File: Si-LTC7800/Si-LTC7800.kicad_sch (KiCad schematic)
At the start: 0 parts

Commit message: Schematics for Si and GaN for LTC7800 controller
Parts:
- added BFET_VGS, TFET_VGS: TestPoint_2Pole, symbol Connector:TestPoint_2Pole
- added C1, C3, C4: 0.1uF, symbol Device:C
- added C2, CinA-1, CinA-2: 2.2uF, symbol Device:C
- added C5: 10pF, symbol Device:C
- added CinB: 56uF, symbol Device:C_US
- added Cout: 100uF, symbol Device:C
- added D1: 1N47xxA, Diode_THT:D_DO-41_SOD81_P10.16mm_Horizontal, symbol Diode:1N47xxA
- added L1: 0.3uH, XGL1010-333MED:IND_XGL1010-333MED, symbol XGL1010-333MED:XGL1010-333MED
- added Q1, Q2: DMP2045U-7, SOT96P240X115-3N, symbol DMP2045U-7:DMP2045U-7
- added R1: 100kOhm, symbol Device:R
- added R2: 25.5kOhm, symbol Device:R
- added R3: 3mOhm, symbol Device:R
- added R4: 100Ohm, symbol Device:R
- added R5: 90.9kOhm, symbol Device:R
- added R6: 280kOhm, symbol Device:R
- added TP_VIN, TP_VOUT: TestPoint, symbol Connector:TestPoint
- added U1: LTC7800HUDC_PBF, LTC7800HUDC_PBF:QFN50P400X300X80-21N, symbol LTC7800HUDC_PBF:LTC7800HUDC_PBF
- added VSource_GND, VSource_IN: 575-4, 5754, symbol 575-4:575-4
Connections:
- new net: L1.2, R3.1, R4.1
- new net: C1.2, U1.19 (TRACK/SS)
- new net: R2.2, U1.20 (FREQ)
- new net: R1.1, U1.9 (PGOOD)
- new net BG: BFET_VGS.1, Q2.1, U1.13 (BG)
- new net BOOST: C3.1, D1.1 (K), U1.12 (BOOST)
- new net GND: BFET_VGS.2, C1.1, C2.1, CinA-1.2, CinA-2.2, CinB.2, Cout.2, Q2.2, R2.1, R5.2, U1.15 (EXTVCC), U1.16 (PGND), U1.2 (SGND), U1.21 (SGND), U1.3 (SGND), VSource_GND.1
- new net INTVCC: C2.2, D1.2 (A), R1.2, U1.14 (INTVCC)
- new net SENSE+: C4.1, R4.2, U1.6 (SENSE+)
- new net SENSE-: C4.2, C5.1, Cout.1, R3.2, R6.1, TP_VOUT.1, U1.5 (SENSE-)
- new net SW: C3.2, L1.1, Q1.2, Q2.3, TFET_VGS.2, U1.11 (SW)
- new net TG: Q1.1, TFET_VGS.1, U1.10 (TG)
- new net VFB: C5.2, R5.1, R6.2, U1.7 (VFB)
- new net VIN: CinA-1.1, CinA-2.1, CinB.1, Q1.3, TP_VIN.1, U1.17 (VIN), VSource_IN.1
- no-connect marks 0 -> 4

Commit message: Updated footprints for LTC7800
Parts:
- removed D1: 1N47xxA, Diode_THT:D_DO-41_SOD81_P10.16mm_Horizontal, symbol Diode:1N47xxA
- added D1: CMPD6001_TR_PBFREE, Diode_SMD:SOT95P230X109-3N, symbol CMPD6001_TR_PBFREE:CMPD6001_TR_PBFREE
- added RLoad1: 5Ohm, Resistor_SMD:R_0201_0603Metric_Pad0.64x0.40mm_HandSolder, symbol Device:R
- BFET_VGS1: renamed from BFET_VGS; footprint (none) -> TestPoint:TestPoint_Bridge_Pitch2.54mm_Drill1.0mm
- C1, C2, C3, C4, C5, CinA-1, CinA-2: footprint (none) -> Capacitor_SMD:C_0805_2012Metric_Pad1.18x1.45mm_HandSolder
- CinB1: renamed from CinB; footprint (none) -> Capacitor_SMD:C_0805_2012Metric_Pad1.18x1.45mm_HandSolder
- Cout1: renamed from Cout; footprint (none) -> Capacitor_SMD:C_0805_2012Metric_Pad1.18x1.45mm_HandSolder
- L1: value 0.3uH -> 33uH; footprint XGL1010-333MED:IND_XGL1010-333MED -> Inductor_SMD:IND_XGL1010-333MED
- Q1, Q2: footprint SOT96P240X115-3N -> Transistor_Power:SOT96P240X115-3N
- R1, R2, R3, R4, R5, R6: footprint (none) -> Resistor_SMD:R_0201_0603Metric_Pad0.64x0.40mm_HandSolder
- TFET_VGS1: renamed from TFET_VGS; footprint (none) -> TestPoint:TestPoint_Bridge_Pitch2.54mm_Drill1.0mm
- TP_VIN1: renamed from TP_VIN; footprint (none) -> TestPoint:TestPoint_Loop_D2.60mm_Drill1.6mm_Beaded
- TP_VOUT1: renamed from TP_VOUT; footprint (none) -> TestPoint:TestPoint_Loop_D2.60mm_Drill1.6mm_Beaded
- U1: footprint LTC7800HUDC_PBF:QFN50P400X300X80-21N -> Package_DFN_QFN:QFN50P400X300X80-21N
- VSource_GND1: renamed from VSource_GND; footprint 5754 -> Battery:5754
- VSource_IN1: renamed from VSource_IN; footprint 5754 -> Battery:5754
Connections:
- net BOOST: now also D1.3 (K)
- net GND: now also RLoad1.2
- net INTVCC: now also D1.1 (A)
- net SENSE-: now also RLoad1.1
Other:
- moved on the sheet: BFET_VGS1, C1, C2, C3, C4, C5, CinA-1, CinA-2, CinB1, Cout1, L1, Q1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

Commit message: Updated shematics
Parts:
- added C6: 100pF, Capacitor_SMD:C_0805_2012Metric_Pad1.18x1.45mm_HandSolder, symbol Device:C
- added CinA-E1, CinA-E10, CinA-E11, CinA-E12, CinA-E13, CinA-E14, CinA-E2, CinA-E3, CinA-E4, CinA-E5, CinA-E6, CinA-E7, CinA-E8, CinA-E9: ~, Capacitor_SMD:C_0805_2012Metric_Pad1.18x1.45mm_HandSolder, symbol Device:C
- added R7: 33kOhm, Resistor_SMD:R_0201_0603Metric_Pad0.64x0.40mm_HandSolder, symbol Device:R
- added R9: 3.92kOhm, Resistor_SMD:R_0201_0603Metric_Pad0.64x0.40mm_HandSolder, symbol Device:R
- C1: value 0.1uF -> 0.05uF
- C5: value 10pF -> 2.2uF
- R5: value 90.9kOhm -> 6.8kOhm
- R6: value 280kOhm -> 2.7kOhm
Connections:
- net BOOST: now also CinA-E8.2
- net GND: now also C5.1, C6.1, CinA-E1.2, CinA-E10.1, CinA-E11.1, CinA-E12.1, CinA-E13.1, CinA-E14.2, CinA-E2.2, CinA-E3.1, CinA-E4.1, CinA-E5.1, CinA-E6.2, CinA-E7.2
- net INTVCC: now also CinA-E7.1
- net SENSE+: now also CinA-E9.2
- net SENSE-: now also CinA-E11.2, CinA-E12.2, CinA-E9.1; no longer C5.1
- net SW: now also CinA-E8.1
- net VFB: now also R7.2; no longer C5.2, R6.2
- net VIN: now also CinA-E1.1, CinA-E14.1, CinA-E2.1, CinA-E4.2, CinA-E5.2, CinA-E6.1
- net at C1.2, U1.19 (TRACK/SS): now also CinA-E3.2
- net ITH: now reaches U1.8 (ITH)
- net ITH: now also C6.2, CinA-E13.2, R9.1
- new net: C5.2, CinA-E10.2, R9.2
- new net: R6.2, R7.1
- no-connect marks 4 -> 3
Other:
- moved on the sheet: C1, C2, C3, C5, CinA-1, CinB1, Cout1, R2, R5, RLoad1, TP_VOUT1

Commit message: Si Schematic Update
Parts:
- removed CinA-E1, CinA-E2, CinA-E4, CinA-E6: ~, Capacitor_SMD:C_0805_2012Metric_Pad1.18x1.45mm_HandSolder, symbol Device:C
- BFET_VGS1, TFET_VGS1: footprint TestPoint:TestPoint_Bridge_Pitch2.54mm_Drill1.0mm -> TestPoint:TestPoint_2Pads_Pitch2.54mm_Drill0.8mm
- renumbered CinA-1 to CinA1, CinA-2 to CinA2, CinA-E3 to E_C1, CinA-E7 to E_C2, CinA-E8 to E_C3, CinA-E9 to E_C4, CinA-E10 to E_C5, CinA-E13 to E_C6, CinA-E14 to Ex_Cin1, CinA-E5 to Ex_Cin2, CinA-E12 to Ex_Cout1, CinA-E11 to Ex_Cout2
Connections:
- net SENSE- renamed Vout
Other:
- moved on the sheet: CinA1, Cout1, Ex_Cin2, Ex_Cout1, Ex_Cout2, RLoad1, TP_VOUT1

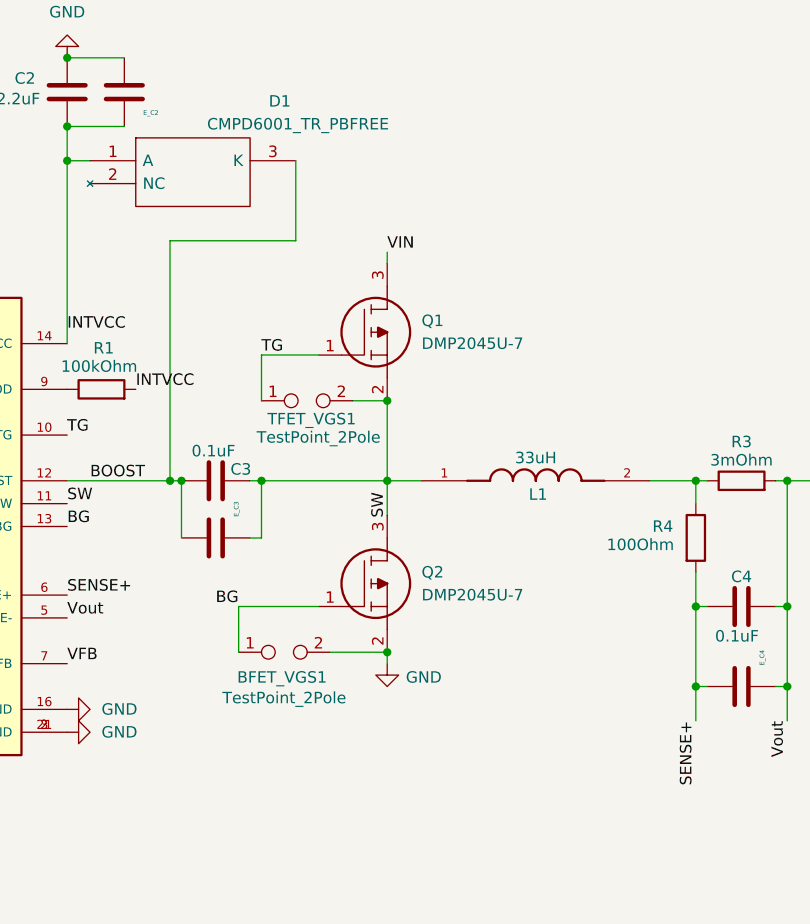
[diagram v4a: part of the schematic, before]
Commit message: Updated MOSFET
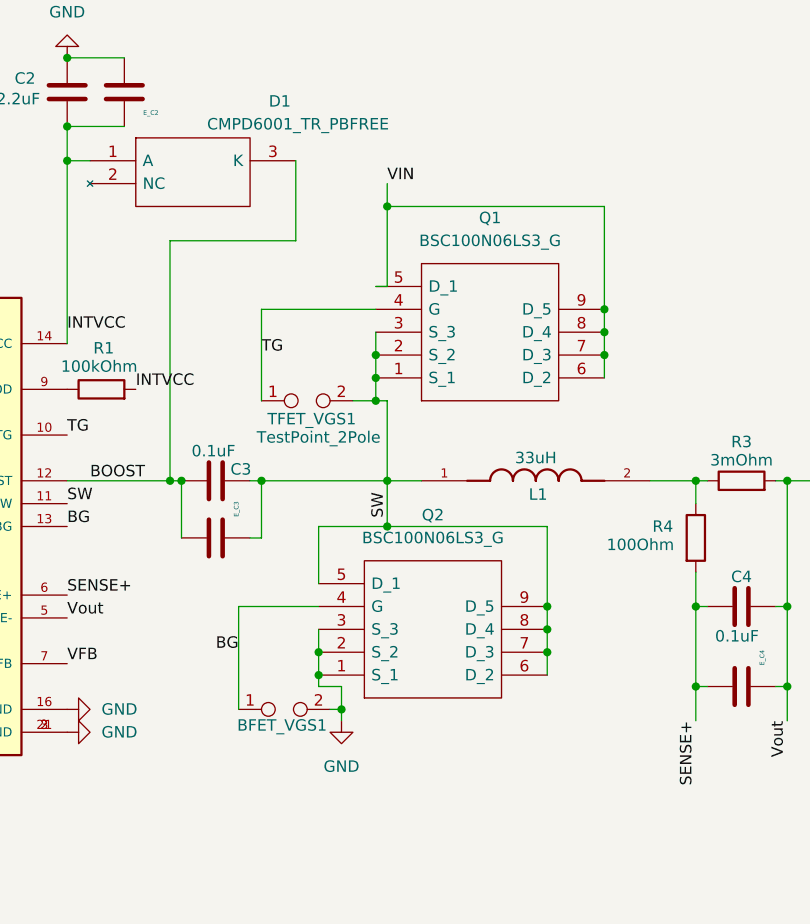
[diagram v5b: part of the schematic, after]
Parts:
- removed Q1, Q2: DMP2045U-7, Transistor_Power:SOT96P240X115-3N, symbol DMP2045U-7:DMP2045U-7
- added Q1, Q2: BSC100N06LS3_G, Transistor_Power:BSC100N06LS3G, symbol BSC100N06LS3_G:BSC100N06LS3_G
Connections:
- net BG: now also Q2.4 (G)
- net GND: now also Q2.1 (S_1), Q2.2 (S_2), Q2.3 (S_3)
- net SW: now also Q1.1 (S_1), Q1.2 (S_2), Q1.3 (S_3), Q2.5 (D_1), Q2.6 (D_2), Q2.7 (D_3), Q2.8 (D_4), Q2.9 (D_5)
- net TG: now also Q1.4 (G)
- net VIN: now also Q1.5 (D_1), Q1.6 (D_2), Q1.7 (D_3), Q1.8 (D_4), Q1.9 (D_5)
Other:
- moved on the sheet: BFET_VGS1

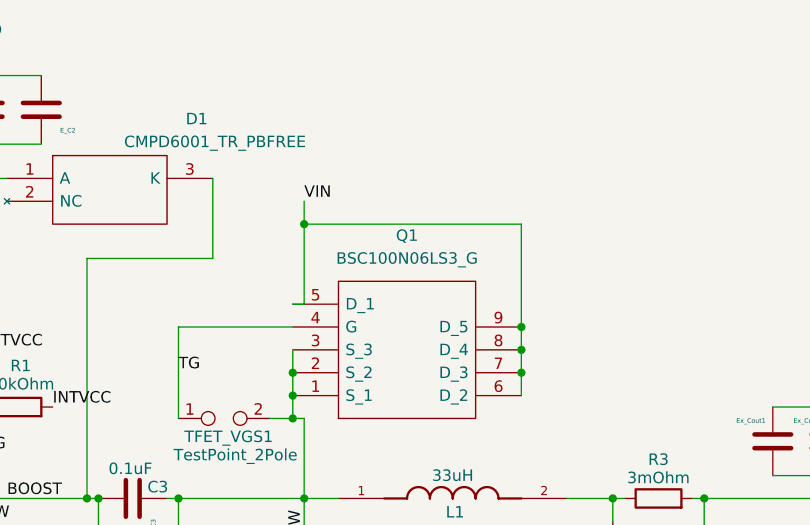
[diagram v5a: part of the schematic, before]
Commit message: FET fixes
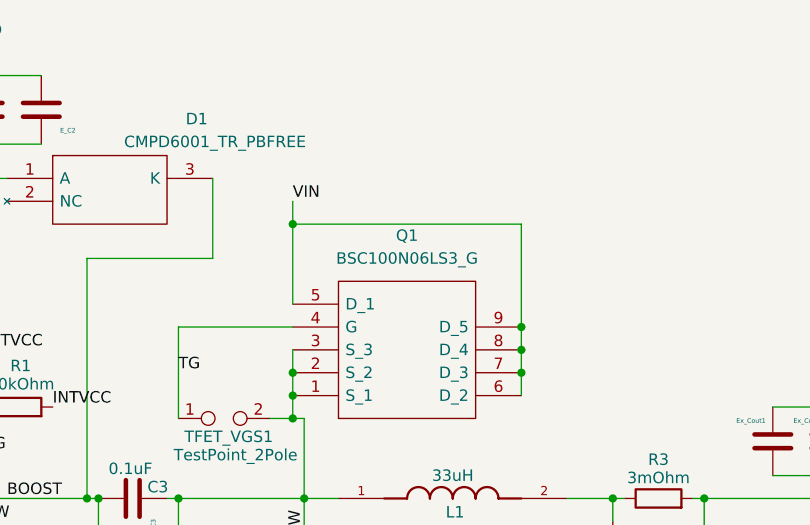
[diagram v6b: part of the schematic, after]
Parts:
- Q1, Q2: footprint Transistor_Power:BSC100N06LS3G -> XT60PW-M:BSC100N06LS3G
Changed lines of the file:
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@@
 	)
 	(junction
-		(at 87.63 82.55)
+		(at 176.53 68.58)
 		(diameter 0)
 		(color 0 0 0 0)
 	)
 	(junction
-		(at 154.94 99.06)
+		(at 87.63 82.55)
 		(diameter 0)
 		(color 0 0 0 0)
 	)
 	(junction
-		(at 177.8 68.58)
+		(at 154.94 99.06)
 		(diameter 0)
 		(color 0 0 0 0)
@@
 	(wire
 		(pts
-			(xy 177.8 66.04) (xy 177.8 68.58)
+			(xy 176.53 66.04) (xy 176.53 68.58)
 		)
 		(stroke
@@
 	(wire
 		(pts
-			(xy 177.8 77.47) (xy 176.53 77.47)
-		)
-		(stroke
-			(width 0)
-			(type default)
-		)
-	)
-	(wire
-		(pts
 			(xy 257.81 99.06) (xy 265.43 99.06)
 		)
@@
 	(wire
 		(pts
-			(xy 201.93 68.58) (xy 177.8 68.58)
+			(xy 176.53 68.58) (xy 201.93 68.58)
 		)
 		(stroke
@@
 	(wire
 		(pts
-			(xy 177.8 68.58) (xy 177.8 77.47)
+			(xy 176.53 68.58) (xy 176.53 77.47)
 		)
 		(stroke
@@
 	)
 	(label "VIN"
-		(at 177.8 66.04 0)
+		(at 176.53 66.04 0)
 		(effects
 			(font
@@
 			)
 		)
-		(property "Footprint" "Transistor_Power:BSC100N06LS3G"
+		(property "Footprint" "XT60PW-M:BSC100N06LS3G"
 			(at 198.12 90.17 0)
 			(effects
@@
 			)
 		)
-		(property "Footprint" "Transistor_Power:BSC100N06LS3G"
+		(property "Footprint" "XT60PW-M:BSC100N06LS3G"
 			(at 191.77 123.19 0)
 			(effects
